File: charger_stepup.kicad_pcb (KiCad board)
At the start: 2 copper layers, 19 parts, among them J1 CONN_in-, J2 CONN_in+, J3 conOut+, J4 conOut-, J5 CONN_bat+, J6 CONN_bat-, U1 TP4056, U2 DW01, U3 FS8205A

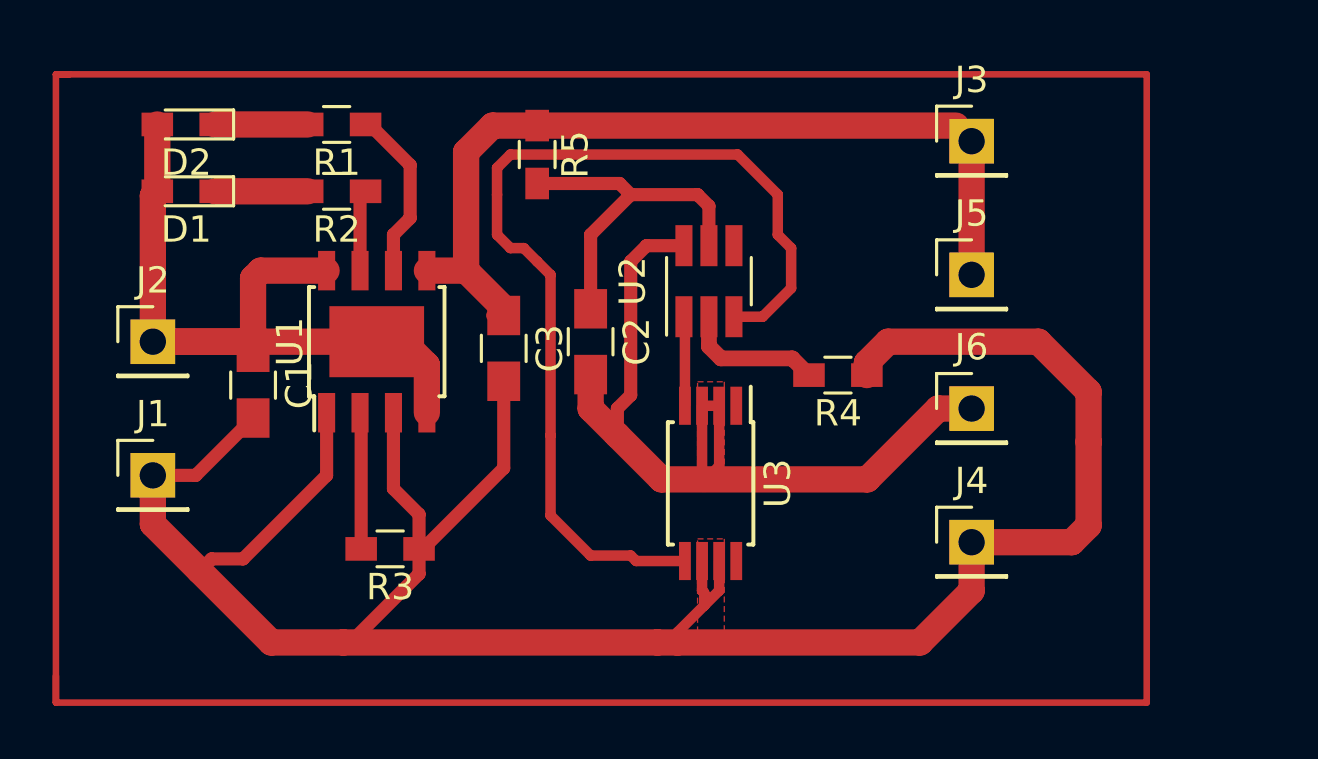
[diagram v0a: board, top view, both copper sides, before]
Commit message: added boost capability with EN reworked PCB generated gerbers and pdf schematic
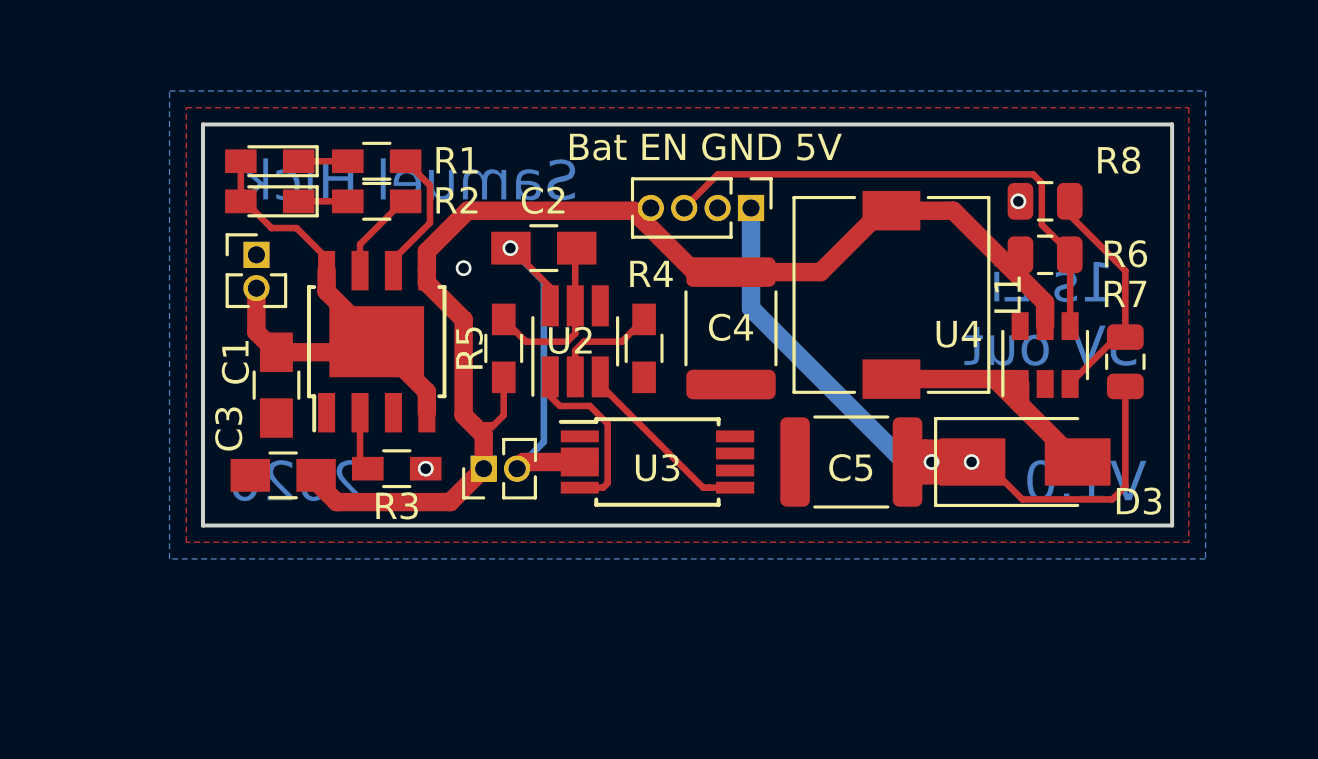
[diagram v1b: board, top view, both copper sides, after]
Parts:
- removed J1: CONN_in-, Pin_Headers:Pin_Header_Straight_1x01_Pitch2.54mm
- removed J2: CONN_in+, Pin_Headers:Pin_Header_Straight_1x01_Pitch2.54mm
- removed J3: conOut+, Pin_Headers:Pin_Header_Straight_1x01_Pitch2.54mm
- removed J4: conOut-, Pin_Headers:Pin_Header_Straight_1x01_Pitch2.54mm
- removed J5: CONN_bat+, Pin_Headers:Pin_Header_Straight_1x01_Pitch2.54mm
- removed J6: CONN_bat-, Pin_Headers:Pin_Header_Straight_1x01_Pitch2.54mm
- added Bat EN GND 5V: Out, Connector_PinHeader_1.27mm:PinHeader_1x04_P1.27mm_Vertical, F.Cu at (142.7, 63.5)
- added Bat-+: Battery, Connector_PinHeader_1.27mm:PinHeader_1x02_P1.27mm_Vertical, F.Cu at (132.6, 73.4)
- added C4: 22uF, Capacitor_SMD:C_1812_4532Metric, F.Cu at (142.0, 68.1)
- added C5: 22uF, Capacitor_SMD:C_1812_4532Metric, F.Cu at (146.6, 73.2)
- added Charge: 5V_Charge, Connector_PinHeader_1.27mm:PinHeader_1x02_P1.27mm_Vertical, F.Cu at (124.0, 65.3)
- added D3: SS34, Diode_SMD:D_SMA, F.Cu at (153.2, 73.2)
- added L1: 22uH, Inductor_SMD:L_7.3x7.3_H4.5, F.Cu at (148.1, 66.8)
- added R6: 10k, Resistor_SMD:R_0805_2012Metric, F.Cu at (153.9, 65.3)
- added R7: 7k5, Resistor_SMD:R_0805_2012Metric, F.Cu at (157.0, 69.3)
- added R8: 1k, Resistor_SMD:R_0805_2012Metric, F.Cu at (153.9, 63.2)
- added U4: MT3608, Package_TO_SOT_SMD:SOT-23-6, F.Cu at (153.9, 69.1)
- U2: value DW01 -> FS312F-G
- moved C3 9.67 mm to (125.0, 73.7), turned to 180 degrees
- moved R5 7.47 mm to (133.3, 68.8), turned to 90 degrees
- moved R4 7.44 mm to (138.7, 68.8), turned to 90 degrees
- moved U2 5.57 mm to (136.1, 68.6)
- moved C2 3.98 mm to (134.9, 65.0), turned to 180 degrees
- moved D2 3.47 mm to (124.5, 61.7)
- moved D1 3.20 mm to (124.5, 63.2)
- moved R3 3.06 mm to (129.3, 73.4)
- moved U3 2.18 mm to (139.2, 73.2), turned to 0 degrees
- moved R1 2.07 mm to (128.5, 61.7)
- moved R2 1.57 mm to (128.5, 63.2)
- moved C1 0.89 mm to (124.7, 70.2)
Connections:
- net IN- renamed GND
- U2 pad 4: (no net) -> Net-(U2-Pad4)
- U3 pad 1: (no net) -> Net-(U3-Pad1)
- U3 pad 8: (no net) -> Net-(U3-Pad8)
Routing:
- net (no net): track 132.2 -> 0.00 mm
- net GND: track 95.3 -> 0.15 mm, vias 0 -> 3
- net Net-(U2-Pad3): track 38.1 -> 7.04 mm
- net 5Vout: track 0.00 -> 30.8 mm, vias 0 -> 2
- net EN: track 0.00 -> 20.2 mm
- net BAT-: track 33.6 -> 15.0 mm, vias 0 -> 1
- net BAT+: track 34.6 -> 51.7 mm
- net Net-(D3-Pad2): track 0.00 -> 10.5 mm
- net IN+: track 30.3 -> 19.9 mm
- net Net-(R7-Pad1): track 0.00 -> 8.88 mm
- net Net-(C2-Pad1): track 13.4 -> 6.47 mm
- net Net-(U2-Pad1): track 3.40 -> 6.74 mm
- net Net-(R3-Pad2): track 5.19 -> 2.25 mm
- net Net-(D2-Pad1): track 3.57 -> 1.86 mm
- net Net-(D1-Pad1): track 3.52 -> 1.86 mm
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- added copper zone on B.Cu, net GND
- removed copper zone on F.Cu, net BAT-
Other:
- board outline added: 36.8 x 15.2 mm
- board text added: "1s Li 5V out"
- board text added: "2020"
- board text added: "Samuel Hick"
- board text added: "V1.0"

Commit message: used correct pinheaders and regernated gerbers
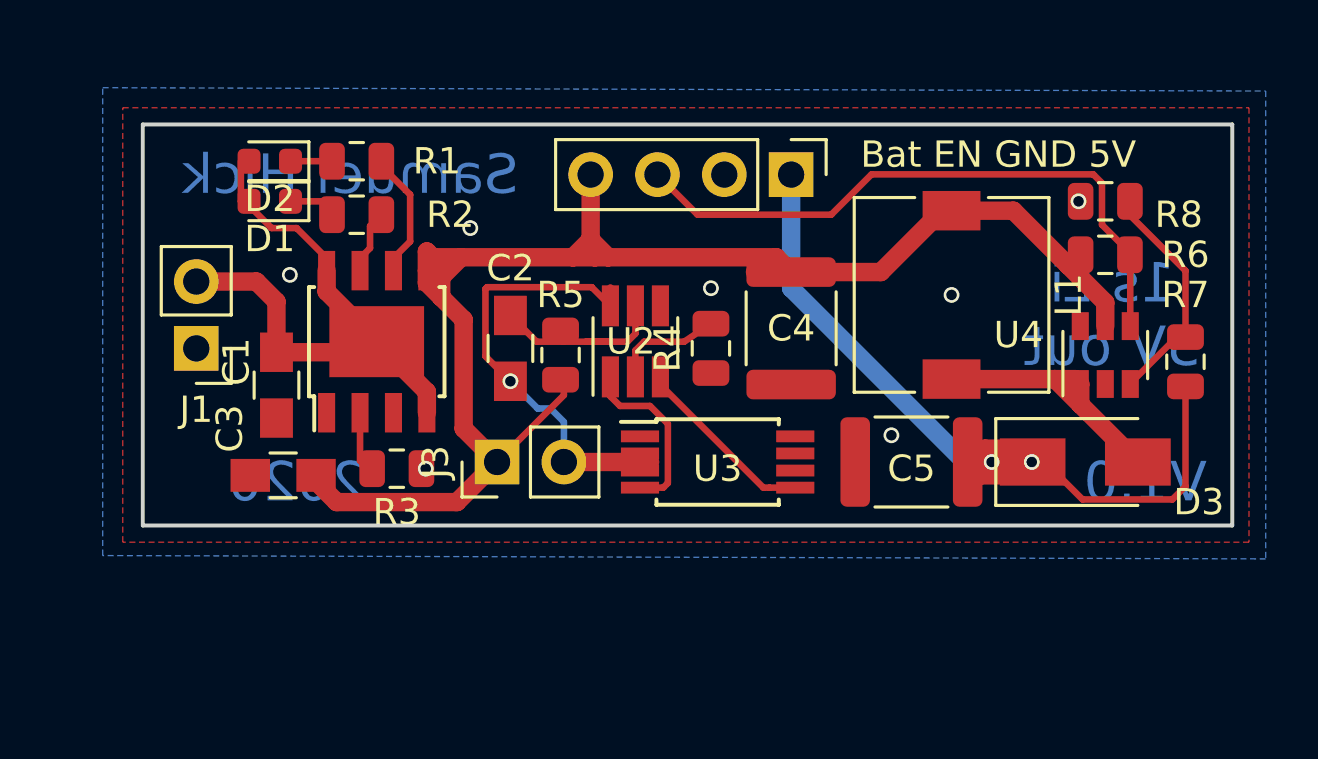
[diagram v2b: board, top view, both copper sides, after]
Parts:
- Bat EN GND 5V: footprint Connector_PinHeader_1.27mm:PinHeader_1x04_P1.27mm_Vertical -> Connector_PinHeader_2.54mm:PinHeader_1x04_P2.54mm_Vertical
- D1, D2: footprint LEDs:LED_0603_HandSoldering -> LED_SMD:LED_0603_1608Metric
- J1: renamed from Charge; footprint Connector_PinHeader_1.27mm:PinHeader_1x02_P1.27mm_Vertical -> Connector_PinHeader_2.54mm:PinHeader_1x02_P2.54mm_Vertical
- J3: renamed from Bat-+; footprint Connector_PinHeader_1.27mm:PinHeader_1x02_P1.27mm_Vertical -> Connector_PinHeader_2.54mm:PinHeader_1x02_P2.54mm_Vertical
- R1, R2, R3, R4, R5: footprint Resistors_SMD:R_0603_HandSoldering -> Resistor_SMD:R_0805_2012Metric
- moved J1 4.23 mm to (121.7, 68.8), turned to 180 degrees
- moved C2 4.02 mm to (133.6, 68.8), turned to 270 degrees
- moved R4 2.54 mm to (141.2, 68.8)
- moved C4 2.29 mm to (144.3, 68.1)
- moved C5 2.29 mm to (148.8, 73.2)
- moved D3 2.29 mm to (155.4, 73.2)
- moved L1 2.29 mm to (150.4, 66.8)
- moved R6 2.29 mm to (156.2, 65.3)
- moved R7 2.29 mm to (159.3, 69.3)
- moved R8 2.29 mm to (156.2, 63.2)
- moved U2 2.29 mm to (138.4, 68.6)
- moved U3 2.29 mm to (141.5, 73.2)
- moved U4 2.29 mm to (156.2, 69.1)
- moved R5 2.17 mm to (135.5, 69.1)
- moved Bat EN GND 5V 1.98 mm to (144.3, 62.2)
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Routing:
- net BAT+: track 51.7 -> 63.0 mm
- net EN: track 20.2 -> 24.3 mm
- net IN+: track 19.9 -> 22.4 mm
- net BAT-: track 15.0 -> 17.1 mm
- net 5Vout: track 30.8 -> 32.4 mm
- net Net-(C2-Pad1): track 6.47 -> 7.94 mm
- net Net-(R2-Pad1): track 3.41 -> 2.46 mm
- net GND: vias 3 -> 7
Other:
- board size 36.8 x 15.2 mm -> 41.4 x 15.2 mm
